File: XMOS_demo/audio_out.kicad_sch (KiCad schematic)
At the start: 39 parts, among them J7 AudioJack3_SwitchT, U2 MAX97220C

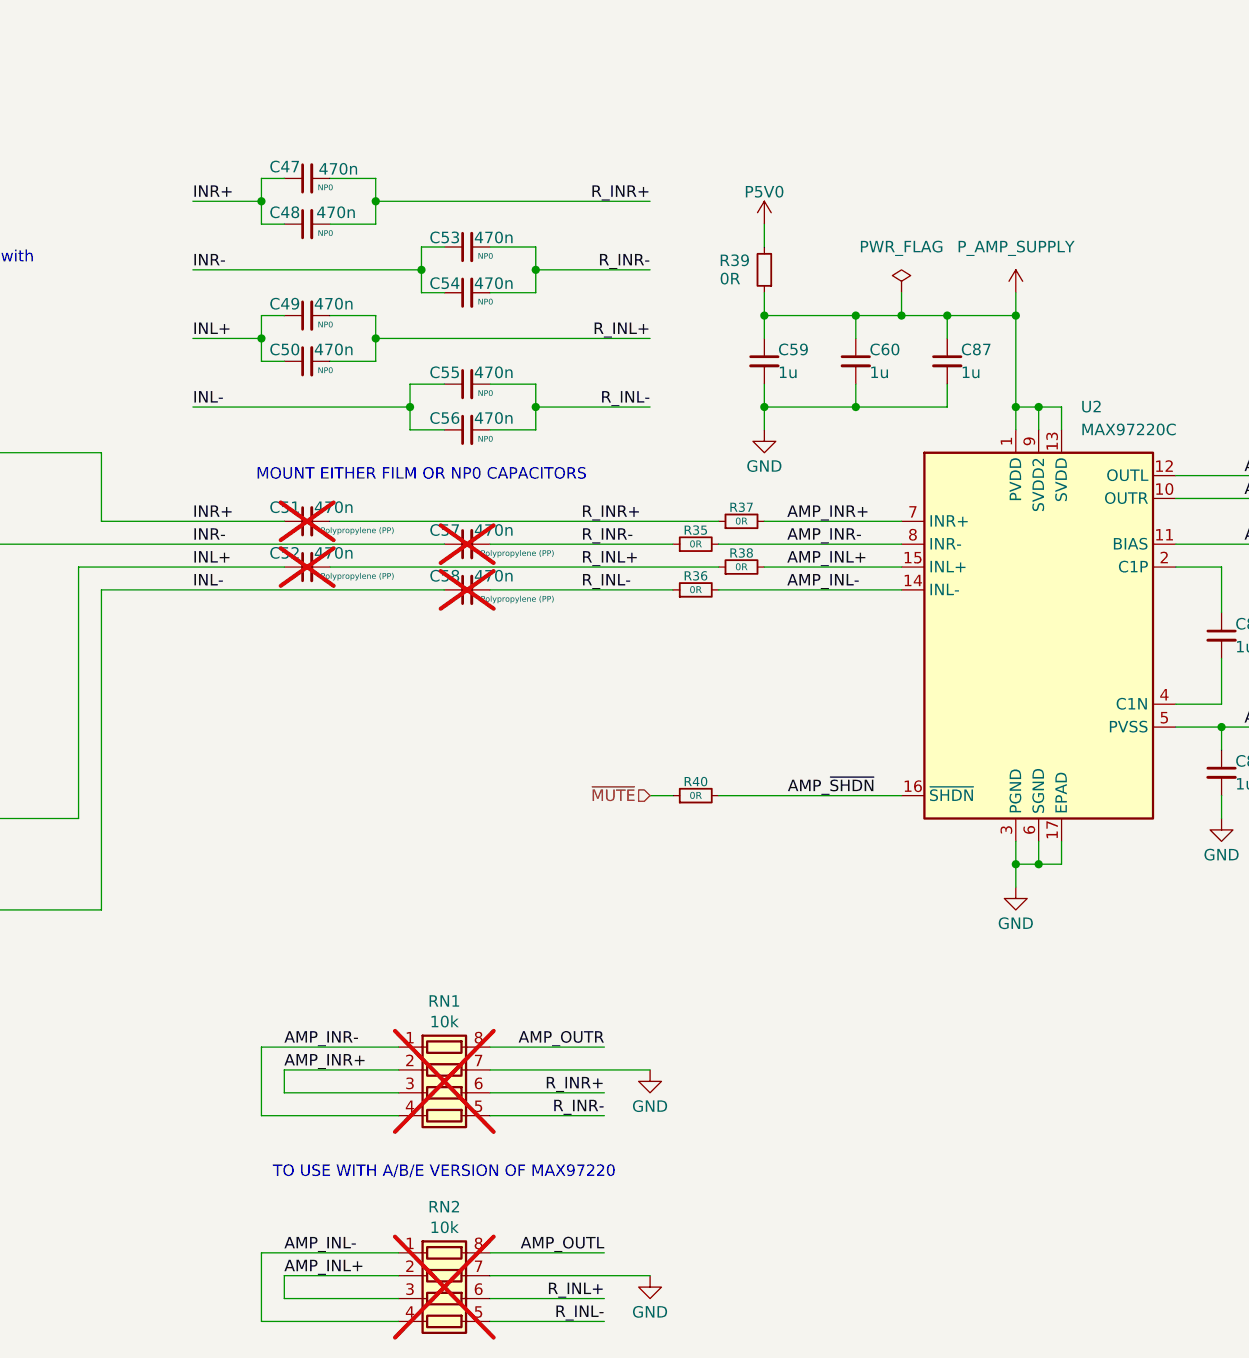
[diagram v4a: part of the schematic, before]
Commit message: work on pcb layout, added active filter to dac out
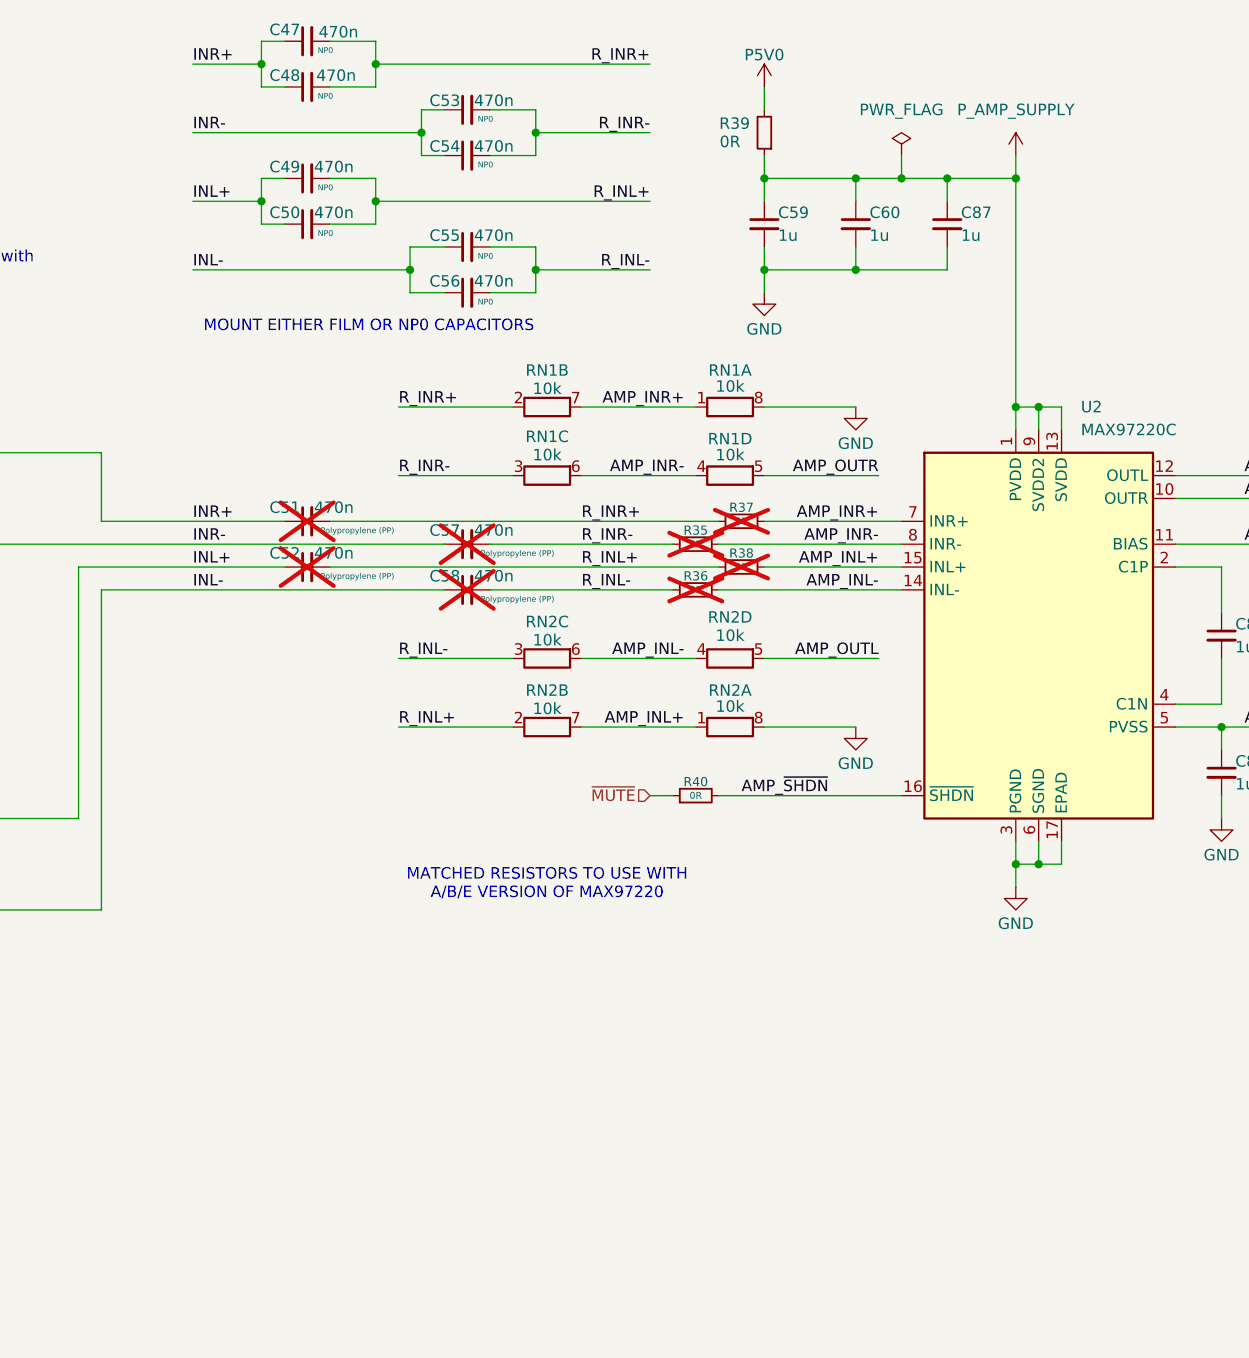
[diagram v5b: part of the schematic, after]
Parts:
- removed RN1, RN2: 10k, Resistor_SMD:R_Array_Convex_4x1206, symbol Device:R_Pack04
- added RN1, RN2: 10k, Resistor_SMD:R_Array_Convex_4x0603, symbol Device:R_Pack04_Split
- C90: footprint Capacitor_SMD:C_0603_1608Metric -> Capacitor_SMD:C_0402_1005Metric
- R35, R36, R37, R38: now not fitted
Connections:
- net AMP_INL+: now also RN2.1 (R1.1), RN2.7 (R2.2)
- net AMP_INL-: now also RN2.4 (R4.1), RN2.6 (R3.2)
- net AMP_INR+: now also RN1.1 (R1.1), RN1.7 (R2.2)
- net AMP_INR-: now also RN1.4 (R4.1), RN1.6 (R3.2)
- net AMP_OUTL: now also RN2.5 (R4.2)
- net AMP_OUTR: now also RN1.5 (R4.2)
- net GND: now also RN1.8 (R1.2), RN2.8 (R1.2)
- net R_INL+: now also RN2.2 (R2.1)
- net R_INL-: now also RN2.3 (R3.1)
- net R_INR+: now also RN1.2 (R2.1)
- net R_INR-: now also RN1.3 (R3.1)
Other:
- note added: "MATCHED RESISTORS TO USE WITH A/B/E VERSION OF MAX97220"
- note removed: "TO USE WITH A/B/E VERSION OF MAX97220"
- moved on the sheet: C47, C48, C49, C50, C53, C54, C55, C56, C59, C60, C87, R39
